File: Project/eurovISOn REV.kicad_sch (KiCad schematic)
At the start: 43 parts, among them IC1 W25Q16JVUXIQ, J1 USB_C_Receptacle_USB2.0, J2 JST SH, J3 Pico EZmate, J5 TC2030_SWD, SW1 boot, SW2 SW_Push, U1 74AHCT1G125, U2 USBLC6-2SC6, U3 RP2040, U4 XC6206PxxxMR-Regulator_Linear, Y1 12MHz

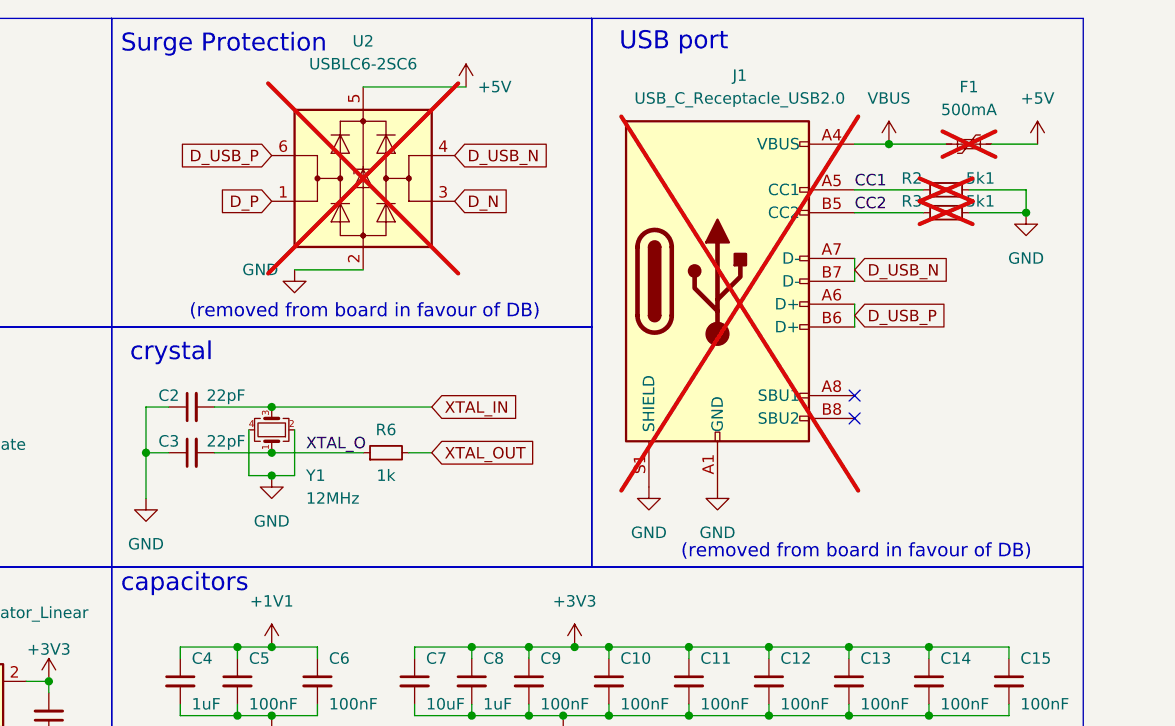
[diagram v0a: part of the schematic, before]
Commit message: rev wip
usb port added
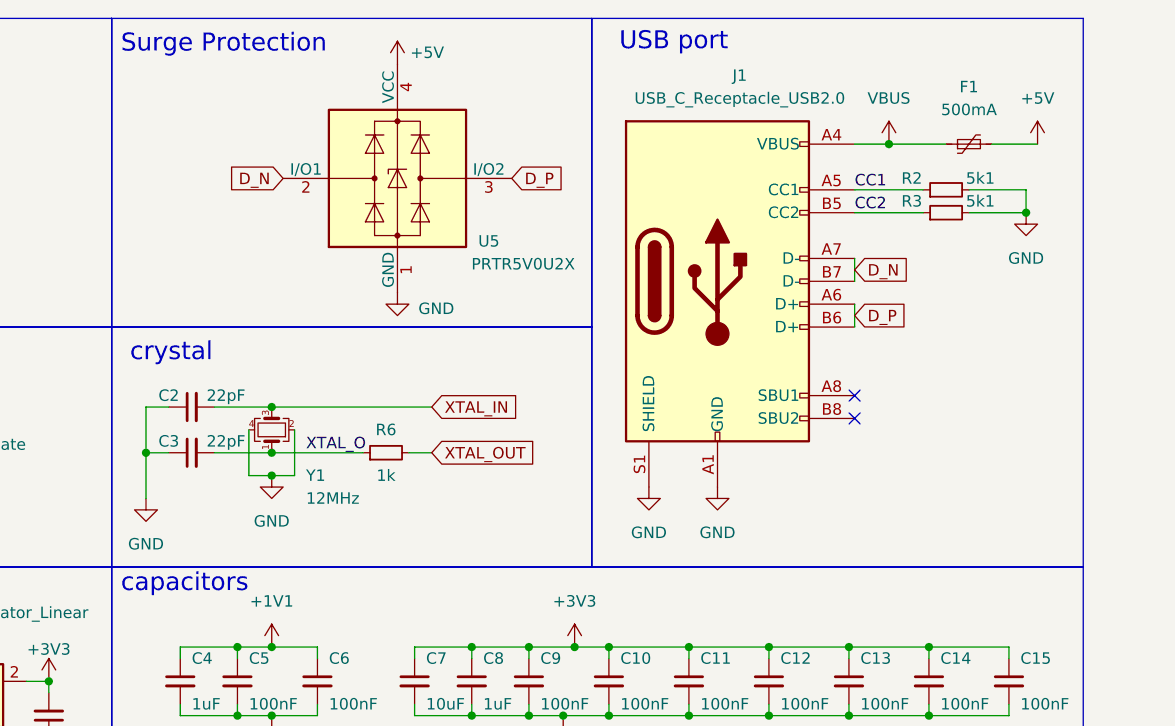
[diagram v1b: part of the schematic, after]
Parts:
- removed U2: USBLC6-2SC6, Package_TO_SOT_SMD:SOT-23-6, symbol Power_Protection:USBLC6-2SC6
- added U5: PRTR5V0U2X, Package_TO_SOT_SMD:SOT-143, symbol Power_Protection:PRTR5V0U2X
- F1, J1, R2, R3: now fitted; now in the parts list
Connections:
- net D_USB_N is gone; now on net D_N: J1.A7 (D-), J1.B7 (D-)
- net D_USB_P is gone; now on net D_P: J1.A6 (D+), J1.B6 (D+)
- net +5V: now also U5.4 (VCC)
- net D_N: now also U5.2 (I/O1)
- net D_P: now also U5.3 (I/O2)
- net GND: now also U5.1 (GND)
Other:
- note removed: "(removed from board in favour of DB)"
